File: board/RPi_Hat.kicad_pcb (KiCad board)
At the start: 2 copper layers, 65 x 56 mm, 42 parts, among them J1 PiHat, SW1 Pushbutton, SW2 Pushbutton, SW3 Pushbutton, SW4 Pushbutton, SW5 Pushbutton, SW6 Pushbutton, SW7 Pushbutton, SW8 Pushbutton

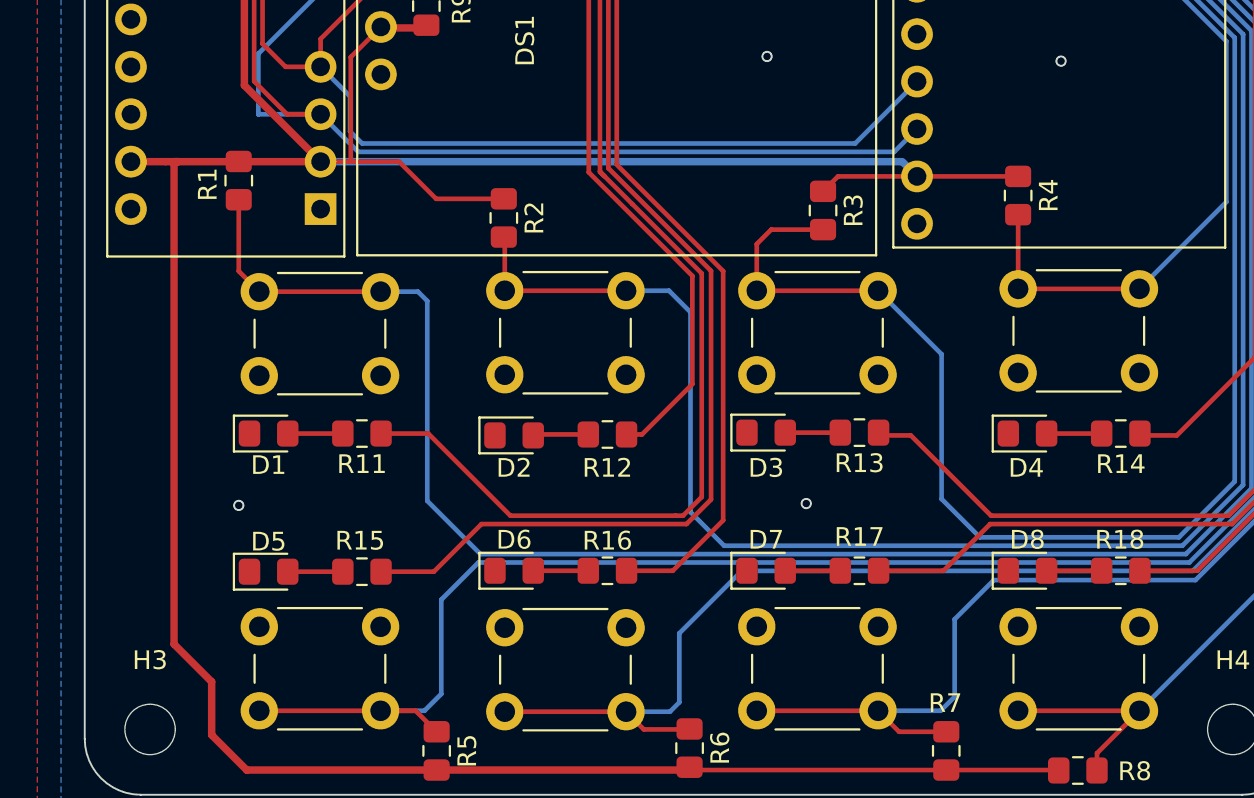
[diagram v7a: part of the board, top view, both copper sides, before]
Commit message: added Diode to monitor SDA
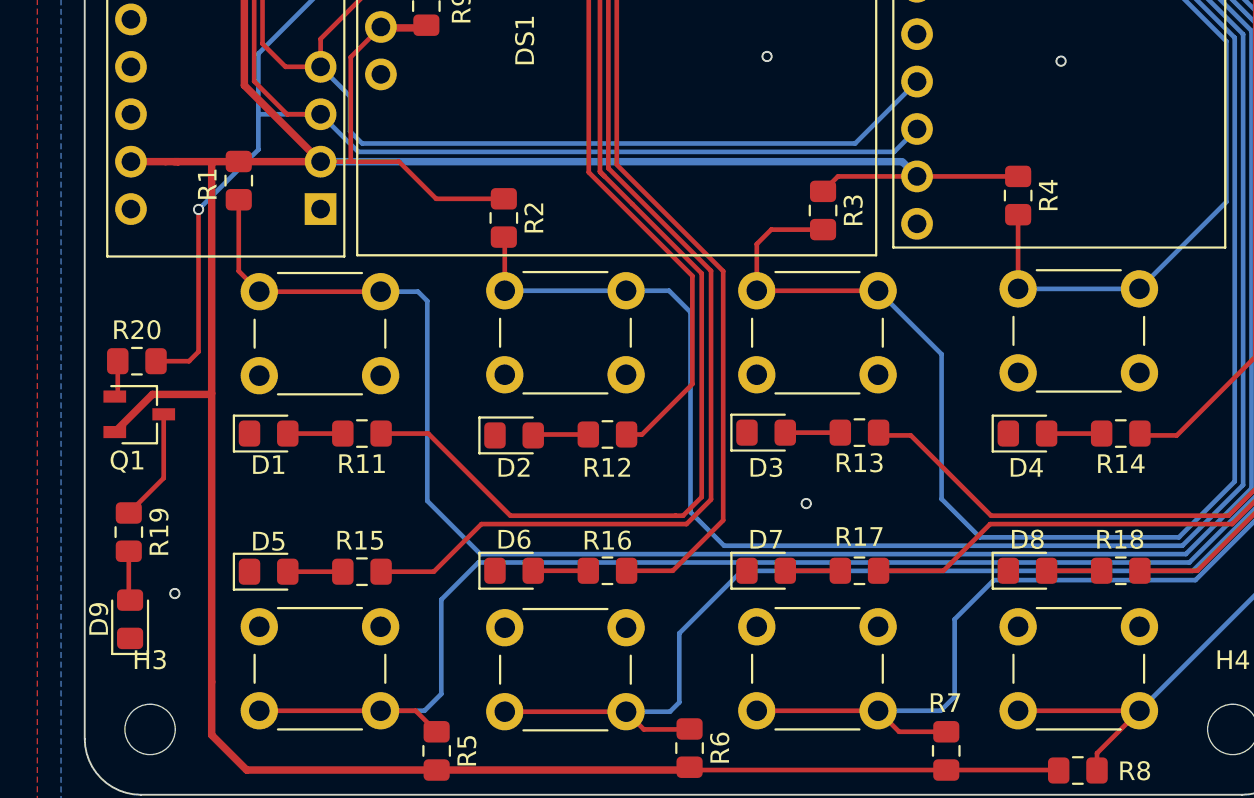
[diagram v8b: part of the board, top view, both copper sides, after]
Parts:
- added D9: green, HWP:LED_0805, F.Cu at (2.43, 47.1)
- added Q1: PMOS_GSD, HWP:SOT-23, F.Cu at (2.92, 36.1)
- added R19: 200, HWP:R_0805, F.Cu at (2.36, 42.4)
- added R20: 100, HWP:R_0805, F.Cu at (2.79, 33.3)
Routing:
- net SDA: track 67.1 -> 83.7 mm, vias 0 -> 1
- net Net-(Q1-Pad3): track 0.00 -> 6.06 mm
- net +3V3: track 192.8 -> 198.0 mm
- net Net-(D9-Pad2): track 0.00 -> 2.65 mm
- net Net-(Q1-Pad1): track 0.00 -> 1.96 mm
